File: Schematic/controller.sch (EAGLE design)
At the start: 32 parts, among them IC1 LM1117-3V3, J1 AVR_SPI_PRG_6NS, Q1 16MHZ, U1 MC34063SMD, U2 ATMEGA328P

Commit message: First completed draft schematic for the controller
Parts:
- removed D3, D4: ZHCS1000TA, adafruit:DIODESOT23_REFLOW
- removed J1: AVR_SPI_PRG_6NS, SparkFun-Connectors:AVR_SPI_PRG_6NS
- added D1: SS14, SparkFun-DiscreteSemi:DIODESMA-ALT
- added IC2: LMV358SOIC, SparkFun-AnalogIC:LMV358SOIC
- added JP3: M02LOCK, SparkFun-Connectors:M02LOCK
- added LED1: RGBLED5050, adafruit:RGBLED5050
- added Q2: MMBT2222A, SparkFun-DiscreteSemi:TRANSISTOR_NPNMMBT2222A
- added Q3: FDN740P, SparkFun-DiscreteSemi:MOSFET-PCHANNEL
- added R10, R11, R12: 220, SparkFun-Resistors:RESISTOR0603
- added R8, R9: 10k, SparkFun-Resistors:RESISTOR0603
- added RV1: (no value), SparkFun-Electromechanical:POT-RV16AF-20
- added S2, S3, S4, S5: SMD-TACT-SWITCH-4, Misc:SMD-TACT-SWITCH-4
- added U$2: M04X2, SparkFun-Connectors:M04X2
- C1: value 1.0uF -> 10uF
- C3: value 470pF -> 330pF; PKG (none) -> 0603
- C4: PKG (none) -> 0603; SOURCE (none) -> http://thegioiic.com/products/0603-22pf-50v-cap
- C5: value 330uF -> 470uF
- C8: value 10uF/16V -> 10uF/6.3V; device SparkFun-Capacitors:22UF-6.3V-20%(0805) -> SparkFun-Capacitors:10UF-6.3V-20%(0603); PKG 0805 -> 0603; SOURCE http://tme.vn/Product.aspx?id=420#page=pro_info -> (none)
- IC1: SOURCE (none) -> http://thegioiic.com/products/ld1117s33ctr
- L1: device SparkFun-Passives:INDUCTOR0805 -> SparkFun-Passives:INDUCTORBOURNS_SRN6045; SOURCE http://tme.vn/Product.aspx?id=1349#page=pro_info -> http://tme.vn/Product.aspx?id=1785#page=pro_info
- R1: PKG (none) -> 0805
- R2: value 1K -> 10k; PKG (none) -> 0603
- R3: value 5.6k -> 33k; PKG (none) -> 0603
- R4: PKG (none) -> 0603
- R5: FOOTPRINT 0805 -> (none); PKG (none) -> 0603; SOURCE (none) -> http://thegioiic.com/products/1-5k-0603-1
- S1: value SWITCH -> SMD-TACT-SWITCH-4; device SparkFun-Electromechanical:SWITCH-MOMENTARY-2SMD-4 -> Misc:SMD-TACT-SWITCH-4
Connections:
- removed net 5V: C7.1, C8.1, D3.C, D4.C, IC1.IN, J1.2, R6.2, U2.AVCC, U2.VCC@1, U2.VCC@2
- removed net 5V_BOOST: C5.+, D4.A, D5.C, R3.1
- new net 5V_REG: C7.1, C8.1, D1.C, IC1.IN, IC2G1.+V, Q3.G, Q3.S, R6.2, R9.1, RV1.A, U2.AVCC, U2.VCC@1, U2.VCC@2
- new net AD0: RV1.S, U2.PC0(ADC0)
- new net AD1: IC2G1.-IN1, IC2G1.OUT1, U2.PC1(ADC1)
- new net AD2: U2.PC2(ADC2)
- new net AD3: U2.PC3(ADC3)
- new net AD4: U2.PC4(ADC4/SDA)
- new net AD5: U2.PC5(ADC5/SCL)
- new net AD6: U2.ADC6
- new net AD7: U2.ADC7
- new net IO10: U$2.4, U2.PB2(SS/OC1B)
- new net IO2: LED1.BLUE_A, U2.PD2(INT0)
- new net IO3: LED1.GREEN_A, U2.PD3(INT1)
- new net IO4: LED1.RED_A, U2.PD4(XCK/T0)
- new net IO5: S2.P$1, U2.PD5(T1)
- new net IO6: S3.P$1, U2.PD6(AIN0)
- new net IO7: S4.P$1, U2.PD7(AIN1)
- new net IO8: S5.P$1, U2.PB0(ICP)
- new net IO9: U$2.3, U2.PB1(OC1A)
- new net N$1: L1.2
- new net N$14: LED1.BLUE_C, R10.1
- new net N$16: LED1.GREEN_C, R11.1
- new net N$17: LED1.RED_C, R12.1
- new net N$21: U$2.8
- new net N$5: Q2.B, R8.2, U1.SWE
- new net VCC: D1.A
- new net V_BOOST: C5.+, D5.C, Q3.D, R3.1
- net 3V3: now also U$2.2
- net GND: now also IC2G1.GND, Q2.E, R10.2, R11.2, R12.2, R8.1, R9.2, RV1.E, S1.P$2, S2.P$2, S3.P$2, S4.P$2, S5.P$2, U$2.1; no longer J1.6, S1.2, U1.SWE
- net MISO: now also U$2.7; no longer J1.1
- net MOSI: now also U$2.6; no longer J1.4
- net N$2: now also Q2.C; no longer L1.2
- net N$6: now also C2.1, JP3.1, R1.1
- net N$8: now also S1.P$1; no longer J1.5, S1.1
- net SCK: now also U$2.5; no longer J1.3
- net V_BAT: now also IC2G1.+IN1, JP3.2
- net V_USB: no longer C2.1, D3.A, R1.1, U1.VCC
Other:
- note added: "CAD note: check footprint of this S1 again"
- note added: "CAD note: find appropriate footprint for this tant cap (2917) and the L1 inductor as well"
- note added: "FW NOTE: need to set pull-up resistors for IO5-8"
- note added: "V_boost = 5V I_out = 250mA"
- note removed: "CAD note: find appropriate footprint for this tant cap (2917)"
- note removed: "CAD note: pick a appropriate switching diode D1"
- note removed: "V_boost = 8V I_out = 250mA"
- moved on the sheet: C3

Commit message: Add initial PCB layout of the controller
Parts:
- Q1: SOURCE (none) -> http://thegioiic.com/products/16mhz-crystal-hc49-dip
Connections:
- net GND: now also LI-PO.1; no longer LI-PO.2
- net N$1: now also D5.A, Q2.C, U1.SWC
- net N$2: now also C2.1, JP3.1, R1.1, U1.VCC; no longer D5.A, Q2.C, U1.SWC
- net N$6: no longer C2.1, JP3.1, R1.1
- net V_BAT: now also LI-PO.2; no longer LI-PO.1
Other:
- moved on the sheet: LI-PO
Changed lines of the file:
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@@
 <layer number="19" name="Unrouted" color="6" fill="1" visible="yes" active="no"/>
 <layer number="20" name="Dimension" color="15" fill="1" visible="yes" active="no"/>
-<layer number="21" name="tPlace" color="16" fill="1" visible="yes" active="no"/>
+<layer number="21" name="tPlace" color="7" fill="1" visible="yes" active="no"/>
 <layer number="22" name="bPlace" color="7" fill="1" visible="yes" active="no"/>
 <layer number="23" name="tOrigins" color="15" fill="1" visible="yes" active="no"/>
@@
 <layer number="49" name="Reference" color="7" fill="1" visible="yes" active="no"/>
 <layer number="50" name="dxf" color="7" fill="1" visible="yes" active="no"/>
-<layer number="51" name="tDocu" color="14" fill="1" visible="yes" active="no"/>
+<layer number="51" name="tDocu" color="7" fill="1" visible="yes" active="no"/>
 <layer number="52" name="bDocu" color="7" fill="1" visible="yes" active="no"/>
 <layer number="53" name="tGND_GNDA" color="7" fill="9" visible="yes" active="no"/>
@@
 <part name="SUPPLY16" library="SparkFun-Aesthetics" deviceset="VCC" device="" value="5V_REG"/>
 <part name="SUPPLY17" library="supply2" deviceset="GND" device=""/>
-<part name="Q1" library="adafruit" deviceset="CRYSTAL" device="HC49S" value="16MHZ"/>
+<part name="Q1" library="adafruit" deviceset="CRYSTAL" device="HC49S" value="16MHZ">
+<attribute name="SOURCE" value="http://thegioiic.com/products/16mhz-crystal-hc49-dip"/>
+</part>
 <part name="C4" library="SparkFun-Capacitors" deviceset="22PF-50V-5%(0603)" device="" value="22pF">
 <attribute name="PKG" value="0603"/>
@@
 <attribute name="NAME" x="165.1" y="98.044" size="1.778" layer="95" rot="R180"/>
 <attribute name="VALUE" x="165.1" y="96.52" size="1.778" layer="96" rot="R180"/>
+<attribute name="SOURCE" x="160.02" y="99.06" size="1.778" layer="96" rot="R90" display="off"/>
 </instance>
 <instance part="C4" gate="G$1" x="152.4" y="101.6" smashed="yes" rot="R90">
@@
 <instance part="SUPPLY22" gate="GND" x="180.34" y="139.7" rot="R90"/>
 <instance part="SUPPLY23" gate="G$1" x="83.82" y="91.44"/>
-<instance part="LI-PO" gate="G$1" x="55.88" y="68.58" rot="R180"/>
+<instance part="LI-PO" gate="G$1" x="40.64" y="68.58"/>
 <instance part="D5" gate="G$1" x="81.28" y="152.4">
 <attribute name="SOURCE" x="81.28" y="152.4" size="1.778" layer="96" display="off"/>
@@
 </busses>
 <nets>
-<net name="N$2" class="0">
-<segment>
-<pinref part="U1" gate="G$1" pin="SWC"/>
-<wire x1="60.96" y1="152.4" x2="71.12" y2="152.4" width="0.1524" layer="91"/>
-<pinref part="D5" gate="G$1" pin="A"/>
-<pinref part="Q2" gate="G$1" pin="C"/>
-<wire x1="71.12" y1="152.4" x2="78.74" y2="152.4" width="0.1524" layer="91"/>
-<junction x="71.12" y="152.4"/>
-</segment>
-</net>
 <net name="GND" class="0">
 <segment>
@@
 <pinref part="U$2" gate="G$1" pin="1"/>
 <wire x1="241.3" y1="43.18" x2="246.38" y2="43.18" width="0.1524" layer="91"/>
-</segment>
-<segment>
-<pinref part="LI-PO" gate="G$1" pin="2"/>
-<pinref part="SUPPLY9" gate="GND" pin="GND"/>
-<wire x1="48.26" y1="66.04" x2="48.26" y2="63.5" width="0.1524" layer="91"/>
 </segment>
 <segment>
@@
 <pinref part="SUPPLY35" gate="GND" pin="GND"/>
 </segment>
+<segment>
+<pinref part="LI-PO" gate="G$1" pin="1"/>
+<pinref part="SUPPLY9" gate="GND" pin="GND"/>
+<wire x1="48.26" y1="68.58" x2="48.26" y2="63.5" width="0.1524" layer="91"/>
+</segment>
 </net>
 <net name="N$6" class="0">
@@
 <pinref part="R2" gate="G$1" pin="1"/>
 <wire x1="40.64" y1="144.78" x2="35.56" y2="144.78" width="0.1524" layer="91"/>
-<wire x1="35.56" y1="144.78" x2="35.56" y2="142.24" width="0.1524" layer="91"/>
 <pinref part="R3" gate="G$1" pin="2"/>
-<wire x1="35.56" y1="142.24" x2="35.56" y2="124.46" width="0.1524" layer="91"/>
+<wire x1="35.56" y1="144.78" x2="35.56" y2="124.46" width="0.1524" layer="91"/>
 <wire x1="35.56" y1="124.46" x2="35.56" y2="121.92" width="0.1524" layer="91"/>
 <wire x1="40.64" y1="124.46" x2="35.56" y2="124.46" width="0.1524" layer="91"/>
-<pinref part="JP3" gate="G$1" pin="1"/>
-<wire x1="15.24" y1="139.7" x2="15.24" y2="142.24" width="0.1524" layer="91"/>
-<pinref part="R1" gate="G$1" pin="1"/>
-<wire x1="15.24" y1="142.24" x2="25.4" y2="142.24" width="0.1524" layer="91"/>
-<pinref part="C2" gate="G$1" pin="1"/>
-<wire x1="25.4" y1="142.24" x2="25.4" y2="137.16" width="0.1524" layer="91"/>
-<wire x1="35.56" y1="142.24" x2="25.4" y2="142.24" width="0.1524" layer="91"/>
-<junction x="25.4" y="142.24"/>
 </segment>
 </net>
@@
 <wire x1="50.8" y1="78.74" x2="48.26" y2="78.74" width="0.1524" layer="91"/>
 <label x="43.18" y="78.74" size="1.778" layer="95"/>
-<pinref part="LI-PO" gate="G$1" pin="1"/>
-<wire x1="48.26" y1="78.74" x2="48.26" y2="68.58" width="0.1524" layer="91"/>
+<pinref part="LI-PO" gate="G$1" pin="2"/>
+<wire x1="48.26" y1="71.12" x2="48.26" y2="78.74" width="0.1524" layer="91"/>
 </segment>
 <segment>
@@
 <wire x1="40.64" y1="149.86" x2="30.48" y2="149.86" width="0.1524" layer="91"/>
 <wire x1="30.48" y1="149.86" x2="30.48" y2="154.94" width="0.1524" layer="91"/>
-<pinref part="L1" gate="G$1" pin="1"/>
 <pinref part="R1" gate="G$1" pin="2"/>
-<wire x1="43.18" y1="160.02" x2="25.4" y2="160.02" width="0.1524" layer="91"/>
 <wire x1="25.4" y1="160.02" x2="25.4" y2="157.48" width="0.1524" layer="91"/>
 <wire x1="25.4" y1="157.48" x2="25.4" y2="154.94" width="0.1524" layer="91"/>
@@
 <pinref part="R7" gate="G$1" pin="1"/>
 <wire x1="25.4" y1="157.48" x2="27.94" y2="157.48" width="0.1524" layer="91"/>
+<pinref part="L1" gate="G$1" pin="1"/>
+<wire x1="43.18" y1="160.02" x2="25.4" y2="160.02" width="0.1524" layer="91"/>
 </segment>
 </net>
@@
 <pinref part="L1" gate="G$1" pin="2"/>
 <wire x1="58.42" y1="160.02" x2="71.12" y2="160.02" width="0.1524" layer="91"/>
-<wire x1="71.12" y1="160.02" x2="71.12" y2="149.86" width="0.1524" layer="91"/>
+<pinref part="D5" gate="G$1" pin="A"/>
+<pinref part="Q2" gate="G$1" pin="C"/>
+<wire x1="71.12" y1="152.4" x2="78.74" y2="152.4" width="0.1524" layer="91"/>
+<pinref part="U1" gate="G$1" pin="SWC"/>
+<wire x1="60.96" y1="152.4" x2="71.12" y2="152.4" width="0.1524" layer="91"/>
+<wire x1="71.12" y1="160.02" x2="71.12" y2="152.4" width="0.1524" layer="91"/>
+<junction x="71.12" y="152.4"/>
 </segment>
 </net>
@@
 </segment>
 </net>
+<net name="N$2" class="0">
+<segment>
+<pinref part="C2" gate="G$1" pin="1"/>
+<pinref part="R1" gate="G$1" pin="1"/>
+<wire x1="25.4" y1="142.24" x2="25.4" y2="137.16" width="0.1524" layer="91"/>
+<junction x="25.4" y="142.24"/>
+<wire x1="15.24" y1="142.24" x2="25.4" y2="142.24" width="0.1524" layer="91"/>
+<pinref part="JP3" gate="G$1" pin="1"/>
+<wire x1="15.24" y1="139.7" x2="15.24" y2="142.24" width="0.1524" layer="91"/>
+<pinref part="U1" gate="G$1" pin="VCC"/>
+<wire x1="40.64" y1="147.32" x2="30.48" y2="147.32" width="0.1524" layer="91"/>
+<wire x1="30.48" y1="147.32" x2="30.48" y2="142.24" width="0.1524" layer="91"/>
+<wire x1="30.48" y1="142.24" x2="25.4" y2="142.24" width="0.1524" layer="91"/>
+</segment>
+</net>
 </nets>
 </sheet>
 </sheets>
+<errors>
+</errors>
 </schematic>
 </drawing>

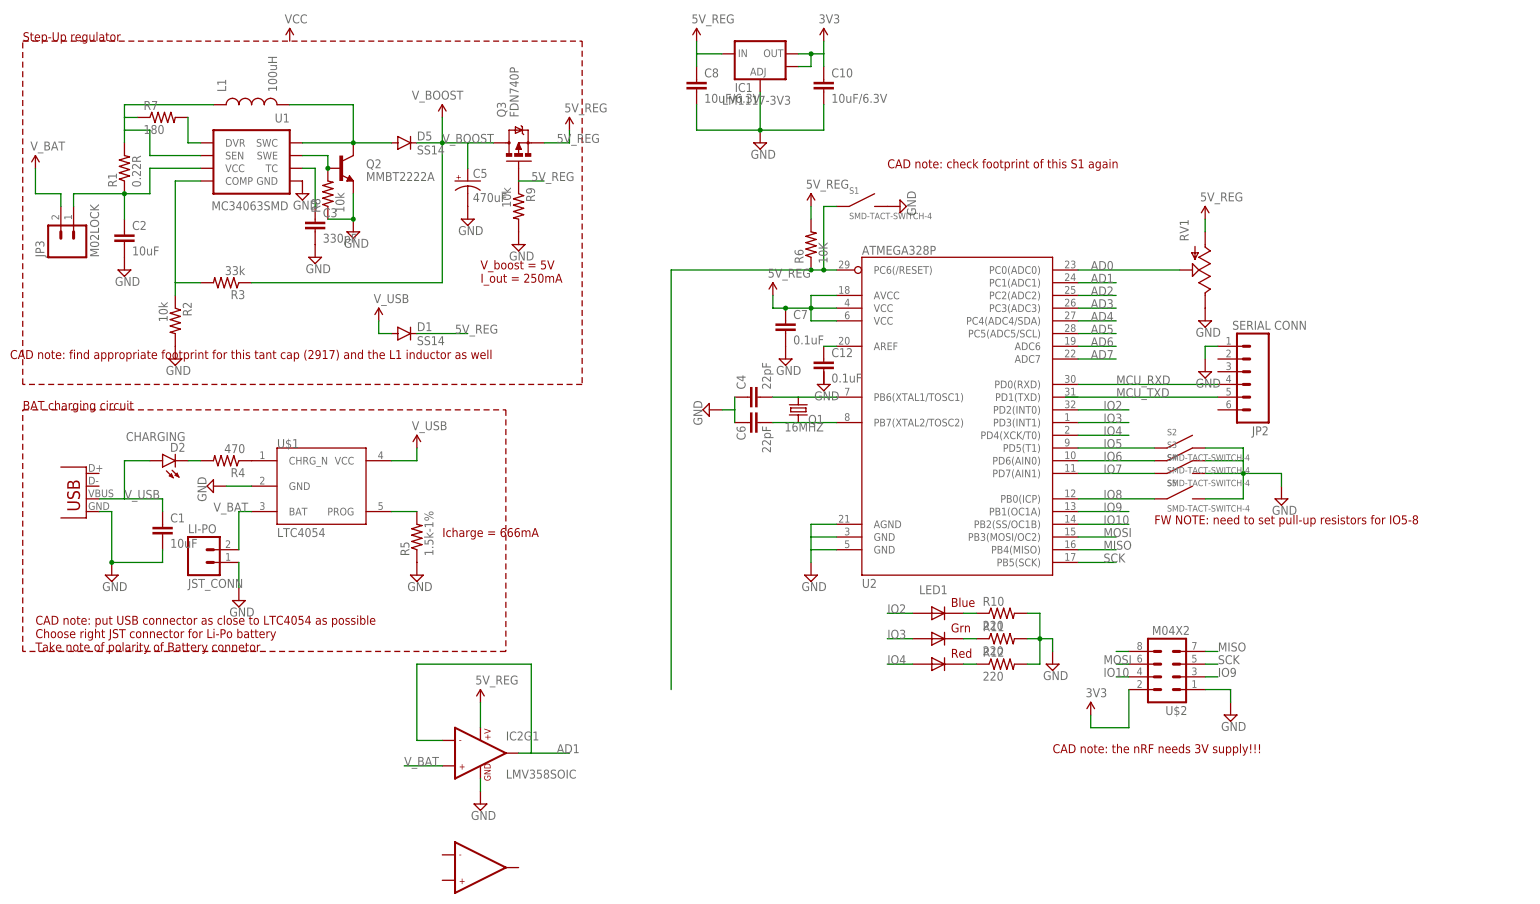
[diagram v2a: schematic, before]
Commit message: Completed layout for the controller
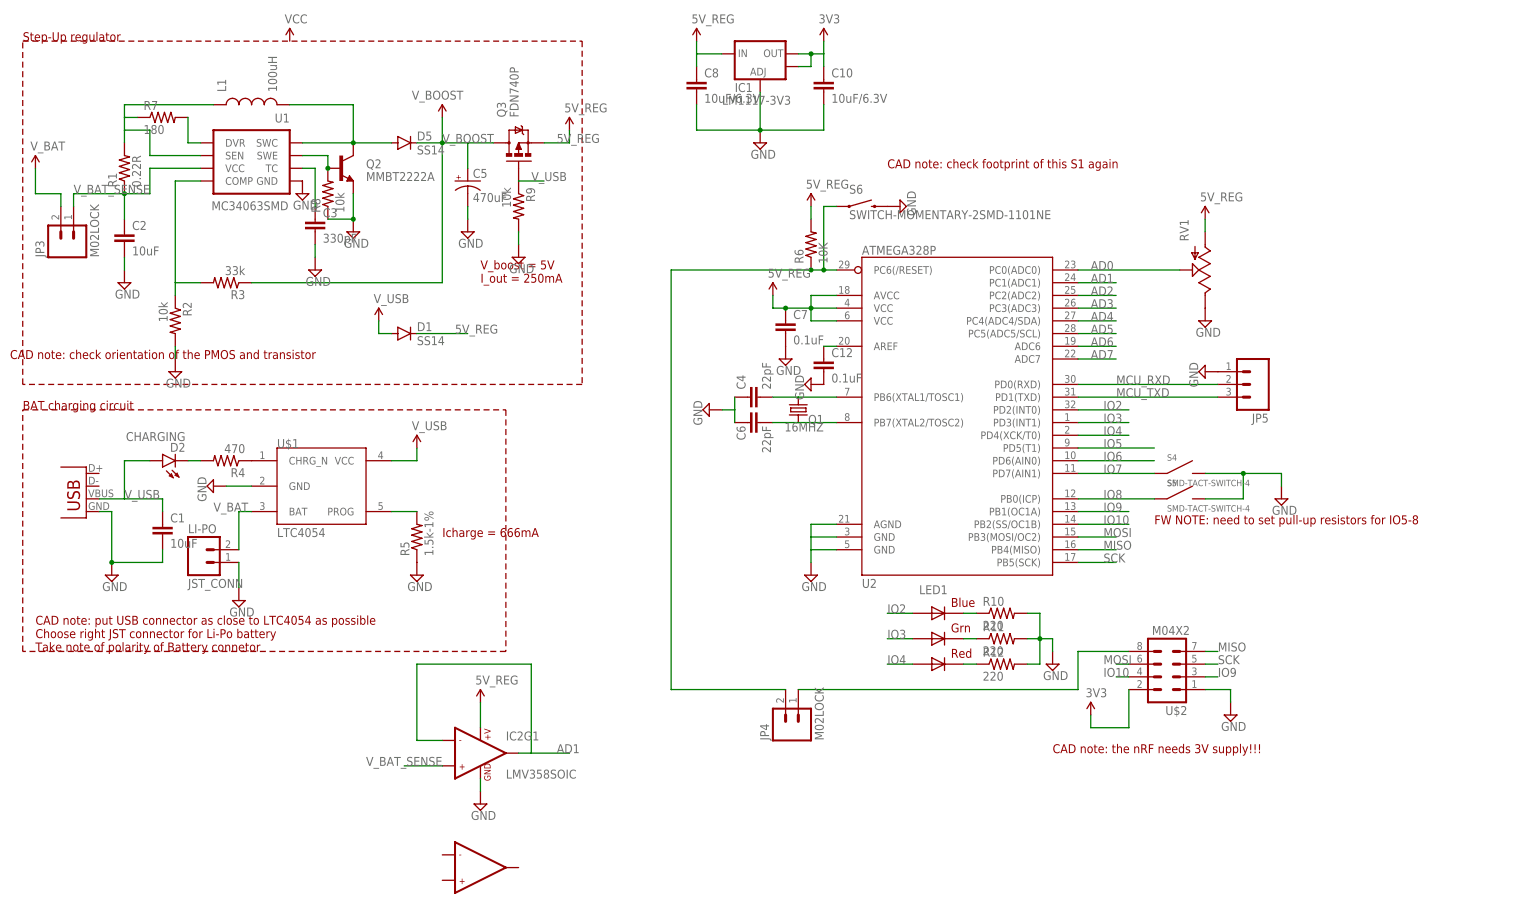
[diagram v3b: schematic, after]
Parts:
- removed JP2: SERIAL CONN, SparkFun-Connectors:M06LOCK
- removed S1, S2, S3: SMD-TACT-SWITCH-4, Misc:SMD-TACT-SWITCH-4
- added JP4: M02LOCK, SparkFun-Connectors:M02LOCK
- added JP5: (no value), SparkFun-Connectors:M03LOCK
- added S6: SWITCH-MOMENTARY-2SMD-1101NE, SparkFun-Electromechanical:SWITCH-MOMENTARY-2SMD-1101NE
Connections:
- net N$1 renamed PWR_L2
- net N$12 renamed PWR_L1
- removed net N$2: C2.1, JP3.1, R1.1, U1.VCC
- removed net VCC: D1.A
- new net V_BAT_SENSE: C2.1, IC2G1.+IN1, JP3.1, R1.1, U1.VCC
- net 5V_REG: no longer Q3.G, R9.1
- net GND: now also C12.2, JP5.1, S6.2; no longer JP2.1, S1.P$2, S2.P$2, S3.P$2
- net IO5: no longer S2.P$1
- net IO6: no longer S3.P$1
- net MCU_RXD: now also JP5.2; no longer JP2.4
- net MCU_TXD: now also JP5.3, U2.PD1(TXD); no longer JP2.5
- net N$21: now also JP4.1
- net N$8: now also JP4.2, S6.1; no longer S1.P$1
- net V_BAT: no longer IC2G1.+IN1
- net V_USB: now also D1.A, Q3.G, R9.1
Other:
- note added: "CAD note: check orientation of the PMOS and transistor"
- note removed: "CAD note: find appropriate footprint for this tant cap (2917) and the L1 inductor as well"
